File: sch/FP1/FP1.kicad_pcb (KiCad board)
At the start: 2 copper layers, 195 x 70 mm, 63 parts, among them J1 240V Mains, J2 Module 0, J3 5VDC, J4 Module 1, J5 Power LED, J6 Connection LED, U1 Electron

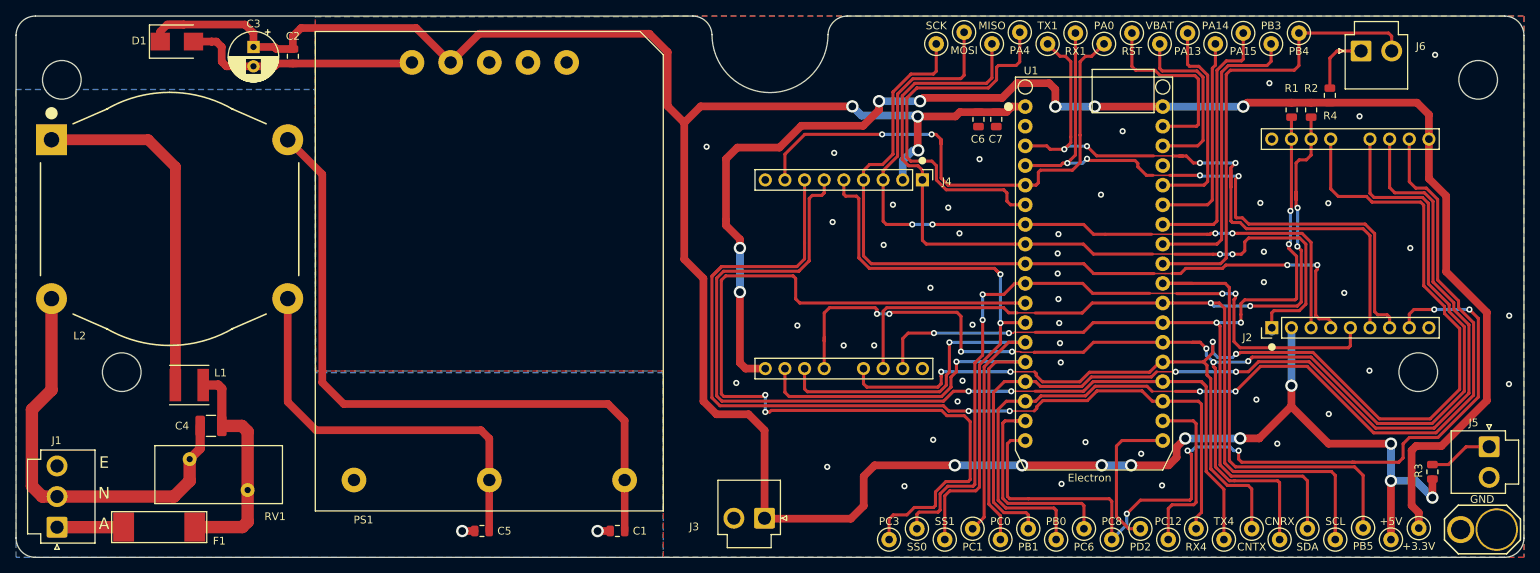
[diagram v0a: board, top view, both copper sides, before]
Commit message: Renamed folders/files as per new coding convention (see README). Added FA1 and FA2 schematics. Updated all schematic title blocks.
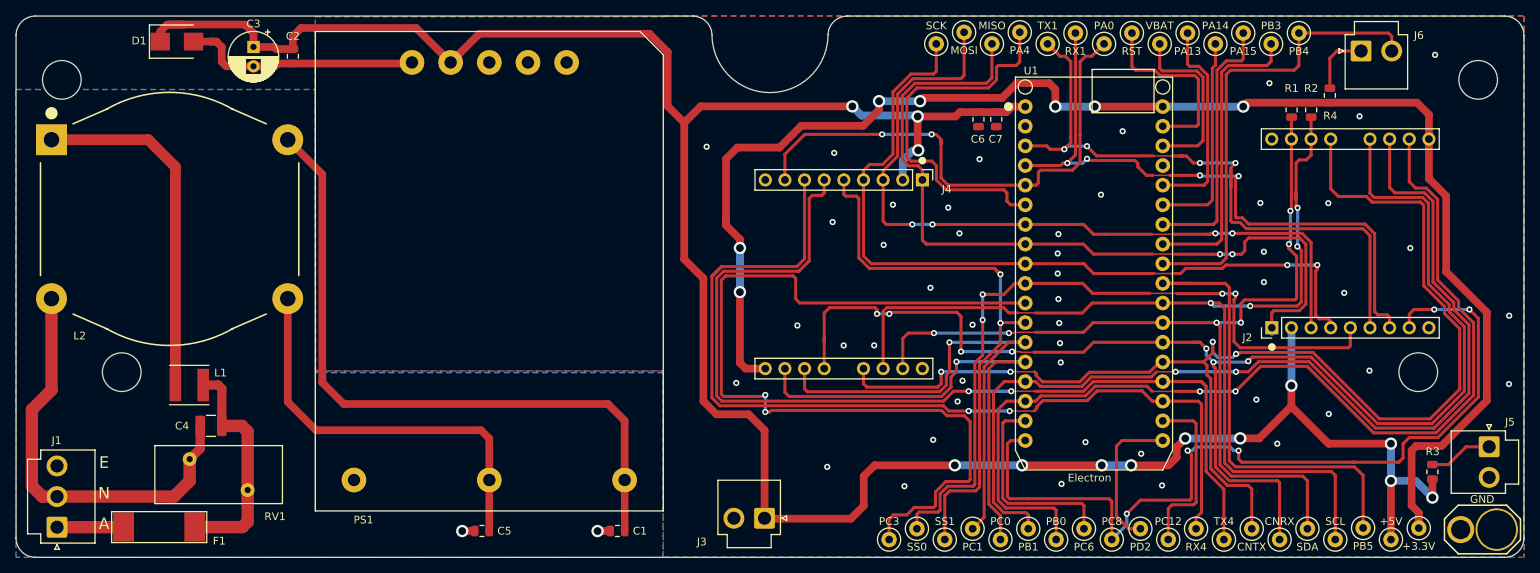
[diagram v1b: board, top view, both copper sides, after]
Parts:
- J2, J4: footprint project_parts:Light_controller_module -> project_parts:Faraday_module
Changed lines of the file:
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@@
   (page A4)
   (title_block
-    (title "Obelisk Light Controller")
+    (title "Faraday FP1")
     (date 3-Oct-2018)
     (rev 0.1)
@@
     (descr "JST VH series connector, B2P-VH (http://www.jst-mfg.com/product/pdf/eng/eVH.pdf), generated with kicad-footprint-generator")
     (tags "connector JST VH side entry")
-    (fp_text reference J5 (at -3.11 2.02) (layer F.SilkS)
+    (fp_text reference J5 (at -3.2 -2.69) (layer F.SilkS)
       (effects (font (size 1 1) (thickness 0.15)))
     )
@@
     (descr "JST VH series connector, B2P-VH (http://www.jst-mfg.com/product/pdf/eng/eVH.pdf), generated with kicad-footprint-generator")
     (tags "connector JST VH side entry")
-    (fp_text reference J6 (at 7.71 -0.6 -180) (layer F.SilkS)
+    (fp_text reference J6 (at 7.47 -2.02 -180) (layer F.SilkS)
       (effects (font (size 1 1) (thickness 0.15)))
     )
@@
     (tags resistor)
     (attr smd)
-    (fp_text reference R3 (at -0.16 1.78 90) (layer F.SilkS)
+    (fp_text reference R3 (at -2.62 -0.03 180) (layer F.SilkS)
       (effects (font (size 1 1) (thickness 0.15)))
     )
@@
       (net 26 "Net-(C4-Pad1)"))
   )
-  (module project_parts:Light_controller_module (layer F.Cu)
+  (module project_parts:Faraday_module (layer F.Cu)
     (at 152.1 90.5 270)
-    (fp_text reference J4 (at -12.1 -13.36) (layer F.SilkS)
+    (fp_text reference J4 (at -11.13 -13.35) (layer F.SilkS)
       (effects (font (size 1 1) (thickness 0.15)))
     )
@@
       (net 4 +5V))
   )
-  (module project_parts:Light_controller_module (layer F.Cu)
+  (module project_parts:Faraday_module (layer F.Cu)
     (at 217.7 85 90)
     (fp_text reference J2 (at -13.58 -13.38 180) (layer F.SilkS)
@@
     (descr "JST VH series connector, B2P-VH (http://www.jst-mfg.com/product/pdf/eng/eVH.pdf), generated with kicad-footprint-generator")
     (tags "connector JST VH side entry")
-    (fp_text reference J3 (at 9.1 -1.1 180) (layer F.SilkS)
-      (effects (font (size 1 1) (thickness 0.15)))
-    )
+    (fp_text reference J3 (at 8.11 -3.05 180) (layer F.SilkS)
+      (effects (font (size 1 1) (thickness 0.15)))
+    )
